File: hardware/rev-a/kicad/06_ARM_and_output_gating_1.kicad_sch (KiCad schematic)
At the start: 16 parts, among them J3 ARM external maintained NO, J4 E-STOP loop NC, K1 HFD27/005-S, K2 HFD27/005-S, K3 HFD27/005-S, K4 HFD27/005-S, Q1 IRLML6344TRPBF

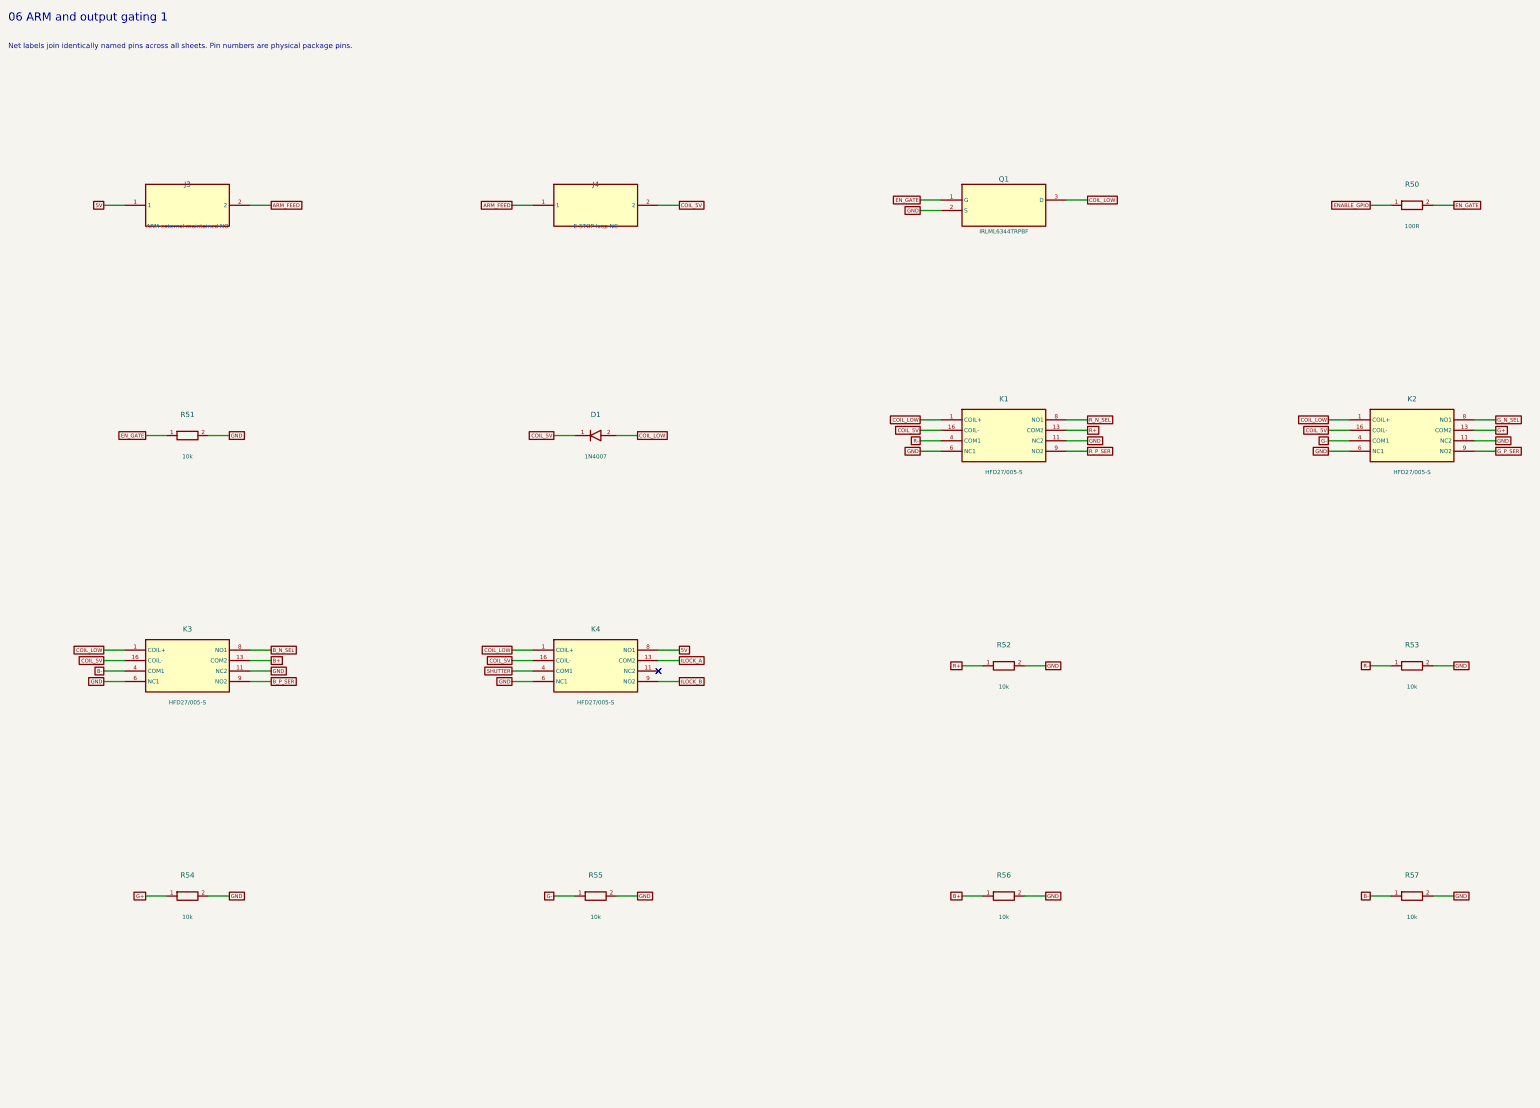
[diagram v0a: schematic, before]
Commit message: Redraw Rev.A schematics with functional blocks and explicit wiring
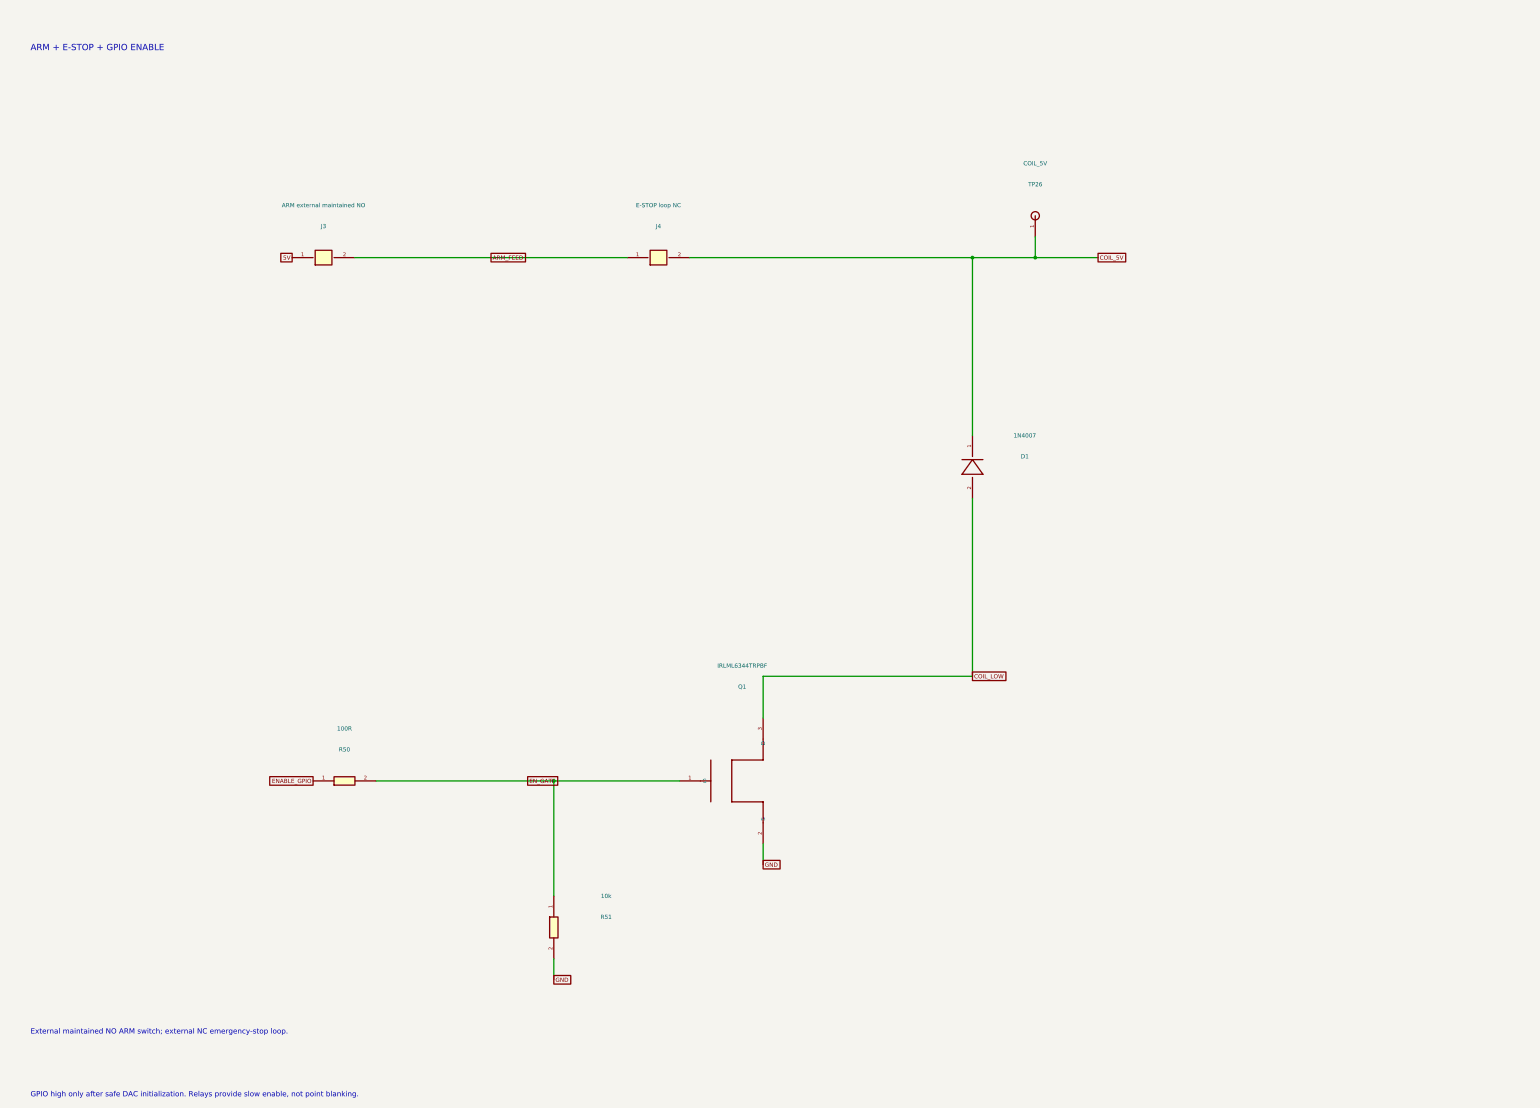
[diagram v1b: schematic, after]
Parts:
- removed K1, K2, K3, K4: HFD27/005-S, RevA:HFD27, symbol RevA:Relay
- removed R52, R53, R54, R55, R56, R57: 10k, RevA:R_Axial_DIN0207_L6.3mm_D2.5mm_P10.16mm_Horizontal, symbol RevA:R
- added TP26: COIL_5V, RevA:TestPoint_THTPad_D2.0mm_Drill1.0mm, symbol RevA:TP
- J3: symbol RevA:Conn_J3 -> RevA:Link
- J4: symbol RevA:Conn_J4 -> RevA:Link
- Q1: symbol RevA:NMOS -> RevA:Part_Q1
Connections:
- net COIL_5V: now also TP26.1
- no-connect marks 1 -> 0
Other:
- note added: "ARM + E-STOP + GPIO ENABLE"
- note added: "External maintained NO ARM switch; external NC emergency-stop loop."
- note added: "GPIO high only after safe DAC initialization. Relays provide slow enable, not point blanking."
- note removed: "06 ARM and output gating 1"
- note removed: "Net labels join identically named pins across all sheets. Pin numbers are physical package pins."
- company: CoreS3 ILDA evaluation -> (none)
- title: 06_ARM_and_output_gating_1 -> 10 / Manual ARM and relay driver
